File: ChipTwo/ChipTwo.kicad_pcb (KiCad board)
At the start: 4 copper layers, 120 x 110 mm, 27 parts, among them J1 Conn_Coaxial, J2 Conn_Coaxial, J3 5767007-8, J4 5767007-8, U1 Y1247AstimulusGenerator, U11 3pinSwitchCustom, U2 Y1247AstimulusGenerator, U3 Y1247AstimulusGenerator, U4 Y1247AstimulusGenerator, U5 CHIP2, U6 3pinSwitchCustom

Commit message: Almost completed with both the chip work
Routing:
- net Net-(J2-Pad1): track 11.7 -> 51.1 mm, vias 0 -> 1
- net Net-(J1-Pad1): track 11.7 -> 48.3 mm, vias 0 -> 1
- net VSS_IO: track 773.5 -> 781.1 mm, vias 4 -> 5

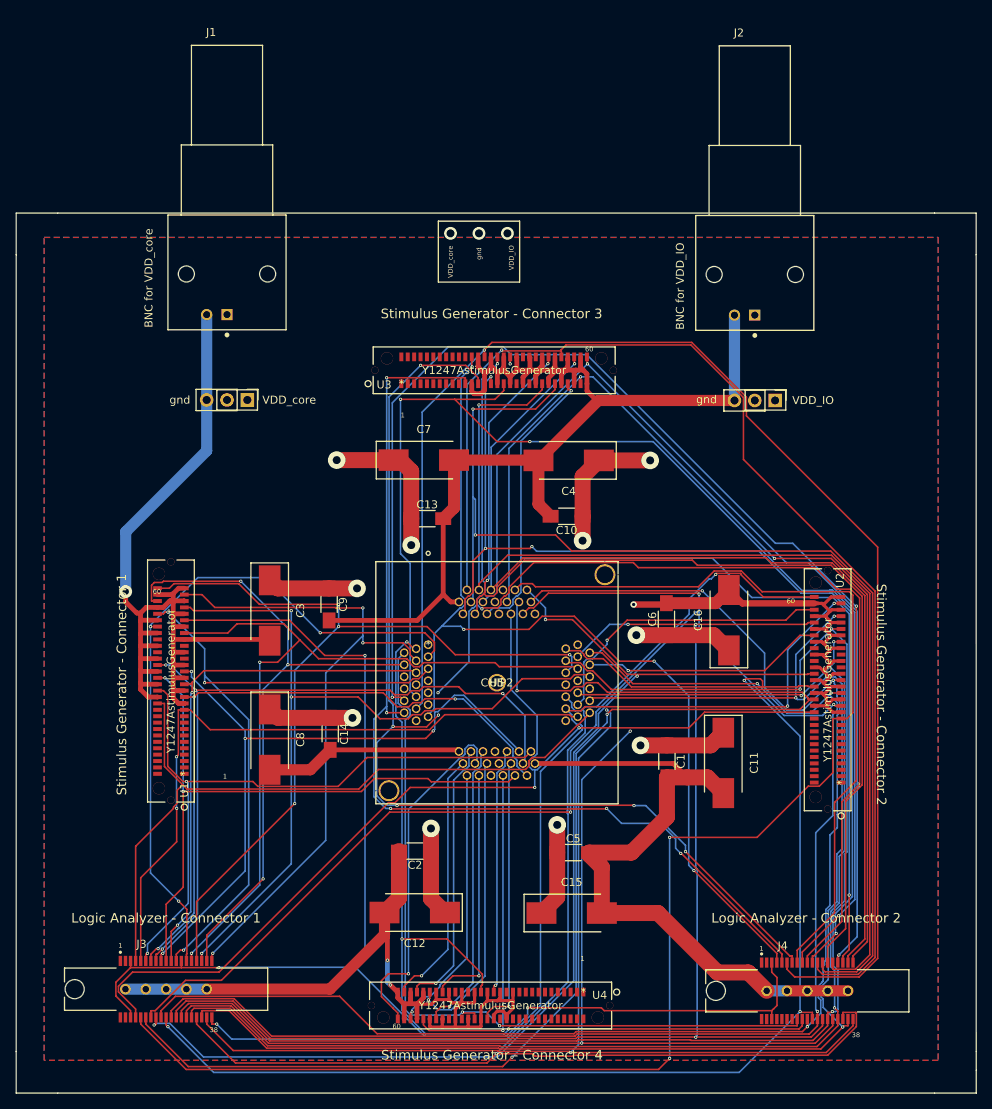
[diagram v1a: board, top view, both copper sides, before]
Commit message: Switch changed in both the layout
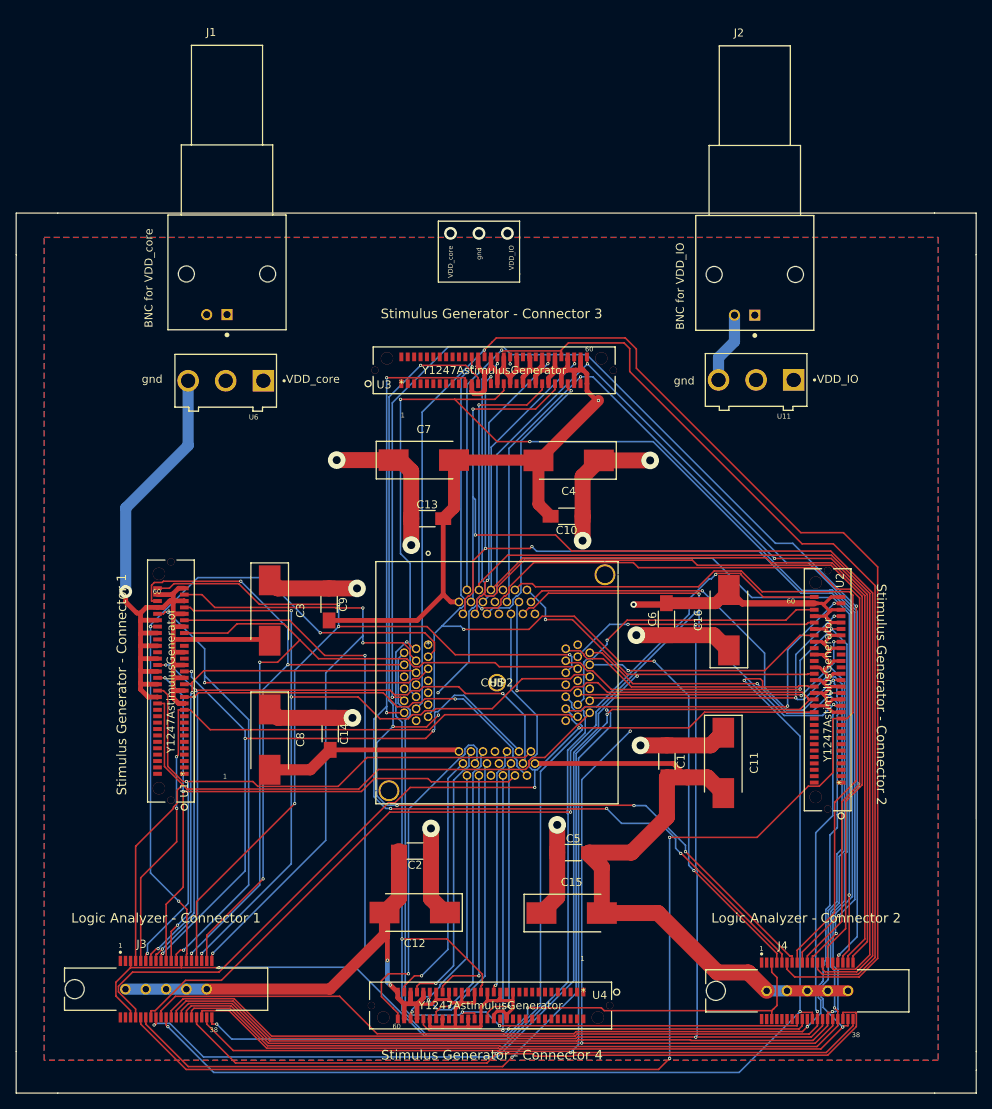
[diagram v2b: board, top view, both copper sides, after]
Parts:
- U11, U6: footprint Pin_Headers:Pin_Header_Straight_1x03_Pitch2.54mm -> SW_MS12ANW03:SW_MS12ANW03
- moved U6 3.61 mm to (48.1, 61.1), turned to 180 degrees
- moved U11 3.50 mm to (114.4, 61.0), turned to 180 degrees
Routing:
- net VDD_IO: track 186.2 -> 188.9 mm
- net VSS_IO: track 781.1 -> 778.5 mm, vias 5 -> 6
- net VDD_core: track 202.9 -> 205.3 mm
- net Net-(J2-Pad1): track 51.1 -> 49.5 mm
- net Net-(J1-Pad1): track 48.3 -> 46.8 mm
- net io[30]: track 151.9 -> 150.4 mm
- net o[5]: track 176.2 -> 175.3 mm

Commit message: Testing for all connections in Chip One is Completed
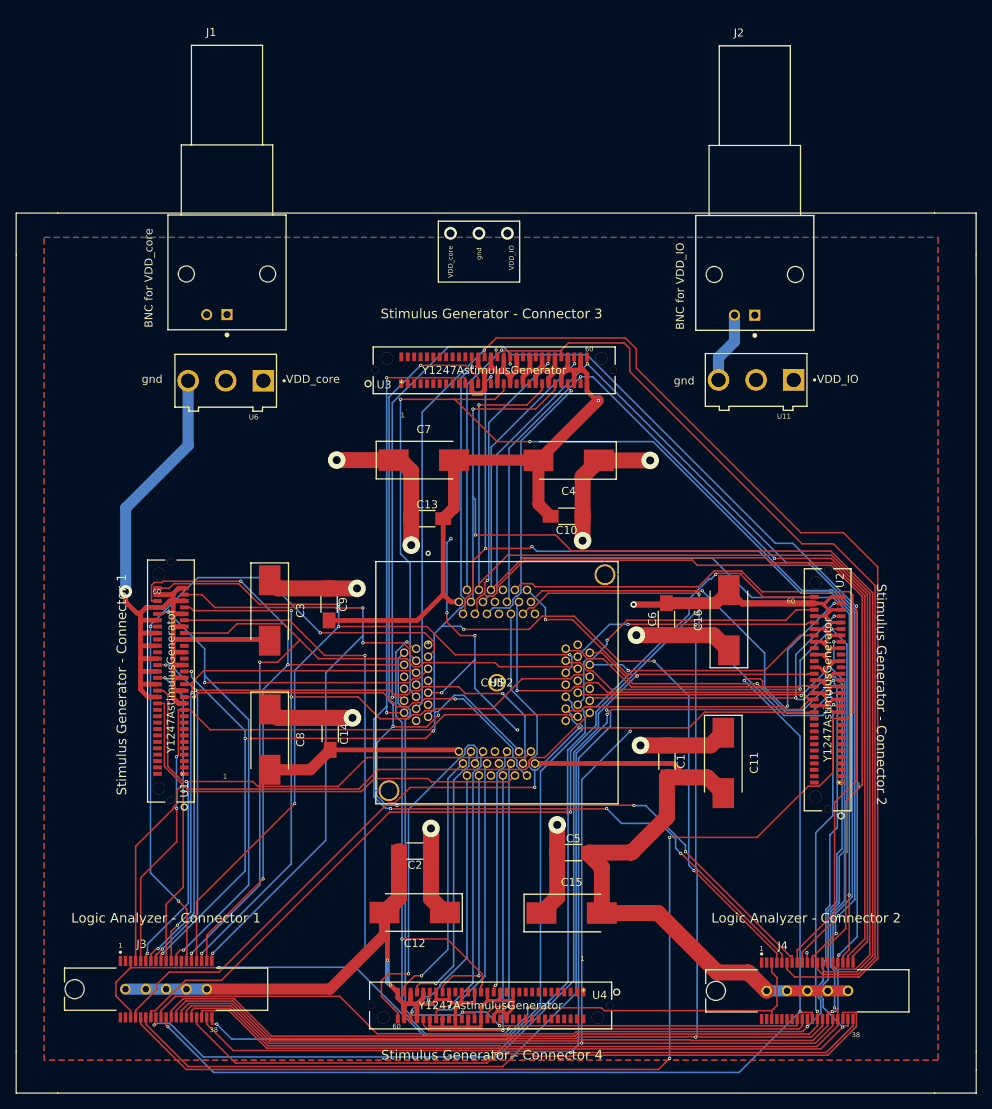
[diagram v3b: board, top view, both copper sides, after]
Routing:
- net o[1]: track 148.1 -> 112.5 mm, vias 3 -> 7
- net io[22]: track 129.1 -> 124.6 mm

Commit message: Checking for chip two completed, Combined PCB updated
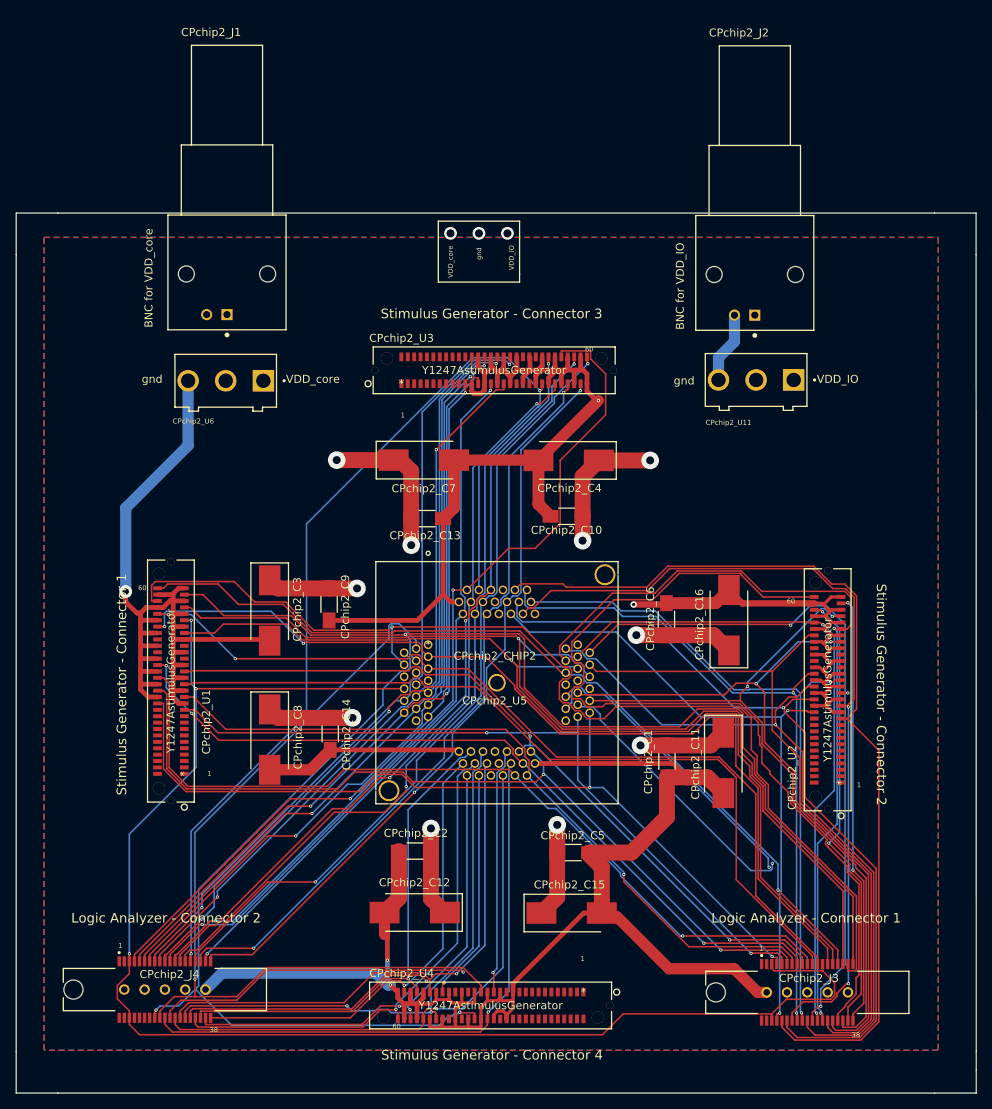
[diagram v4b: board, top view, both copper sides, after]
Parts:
- removed C12: 100uF, Capacitors_Tantalum_SMD:CP_Tantalum_Case-X_EIA-7343-43_Hand
- removed C13: 10uF, Capacitors_SMD:C_1206_HandSoldering
- removed J4: 5767007-8, U4164AlogicAnalyser:TE_5767007-8
- removed U3: Y1247AstimulusGenerator, Y1247AstimulusGenerator:ERF8-030-05.0-L-DV-L-TR
- added CPchip2_C12: 100uF, Capacitors_Tantalum_SMD:CP_Tantalum_Case-X_EIA-7343-43_Hand, F.Cu at (71.7, 127.6)
- added CPchip2_C13: 10uF, Capacitors_SMD:C_1206_HandSoldering, F.Cu at (73.3, 78.3)
- added CPchip2_J4: 5767007-8, U4164AlogicAnalyser:TE_5767007-8, F.Cu at (40.5, 137.2)
- added CPchip2_U3: Y1247AstimulusGenerator, Y1247AstimulusGenerator:ERF8-030-05.0-L-DV-L-TR, F.Cu at (70.1, 61.5)
- CPchip2_U5: renamed from U5; value CHIP2 -> CPchip2_CHIP2
- moved CPchip2_J3 80.2 mm to (120.8, 137.6)
- renumbered C1 to CPchip2_C1, C10 to CPchip2_C10, C11 to CPchip2_C11, C14 to CPchip2_C14, C15 to CPchip2_C15, C16 to CPchip2_C16, C2 to CPchip2_C2, C3 to CPchip2_C3, C4 to CPchip2_C4, C5 to CPchip2_C5, C6 to CPchip2_C6, C7 to CPchip2_C7, C8 to CPchip2_C8, C9 to CPchip2_C9, J1 to CPchip2_J1, J2 to CPchip2_J2, J3 to CPchip2_J3, U1 to CPchip2_U1, U11 to CPchip2_U11, U2 to CPchip2_U2, U4 to CPchip2_U4, U6 to CPchip2_U6
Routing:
- net io[17]: track 180.8 -> 85.2 mm, vias 3 -> 2
- net io[9]: track 177.6 -> 87.7 mm, vias 3 -> 2
- net io[14]: track 168.7 -> 83.8 mm, vias 3 -> 2
- net io[11]: track 168.9 -> 89.5 mm, vias 3 -> 2
- net o[5]: track 175.3 -> 96.1 mm, vias 1 -> 2
- net io[12]: track 164.9 -> 86.1 mm, vias 3 -> 0
- net io[16]: track 169.1 -> 90.4 mm, vias 3 -> 1
- net io[8]: track 176.7 -> 98.3 mm
- net io[13]: track 178.4 -> 100.2 mm, vias 3 -> 2
- net io[15]: track 163.3 -> 88.0 mm
- net io[21]: track 190.3 -> 116.5 mm, vias 2 -> 0
- net io[20]: track 172.9 -> 101.5 mm, vias 3 -> 1
- net o[2]: track 159.8 -> 91.4 mm, vias 3 -> 2
- net io[10]: track 181.2 -> 113.7 mm, vias 2 -> 0
- net o[3]: track 162.6 -> 98.3 mm, vias 3 -> 2
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
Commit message: Both Chips final modification done
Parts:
- moved CPchip2_C1 1.41 mm to (102.3, 107.7)
- moved CPchip2_C10 1.41 mm to (89.7, 77.0)
- moved CPchip2_C11 1.41 mm to (109.3, 107.9)
- moved CPchip2_C12 1.41 mm to (70.7, 126.6)
- moved CPchip2_C13 1.41 mm to (72.3, 77.3)
- moved CPchip2_C14 1.41 mm to (60.2, 104.2)
- moved CPchip2_C15 1.41 mm to (90.3, 126.6)
- moved CPchip2_C16 1.41 mm to (110.0, 90.0)
- moved CPchip2_C2 1.41 mm to (70.8, 118.9)
- moved CPchip2_C3 1.41 mm to (52.6, 88.8)
- moved CPchip2_C4 1.41 mm to (90.0, 70.1)
- moved CPchip2_C5 1.41 mm to (90.5, 119.1)
- moved CPchip2_C6 1.41 mm to (102.2, 89.9)
- moved CPchip2_C7 1.41 mm to (71.9, 70.0)
- moved CPchip2_C8 1.41 mm to (52.6, 105.0)
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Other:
- board size 120 x 110 mm -> 111 x 105 mm
